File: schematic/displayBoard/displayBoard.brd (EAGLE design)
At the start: 65 x 65 mm, 30 parts, among them IC1 4028D, T1 MMBTA42, T10 MMBTA42, T2 MMBTA42, T3 MMBTA42, T4 MMBTA42, T5 MMBTA42, T6 MMBTA42, T7 MMBTA42, T8 MMBTA42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

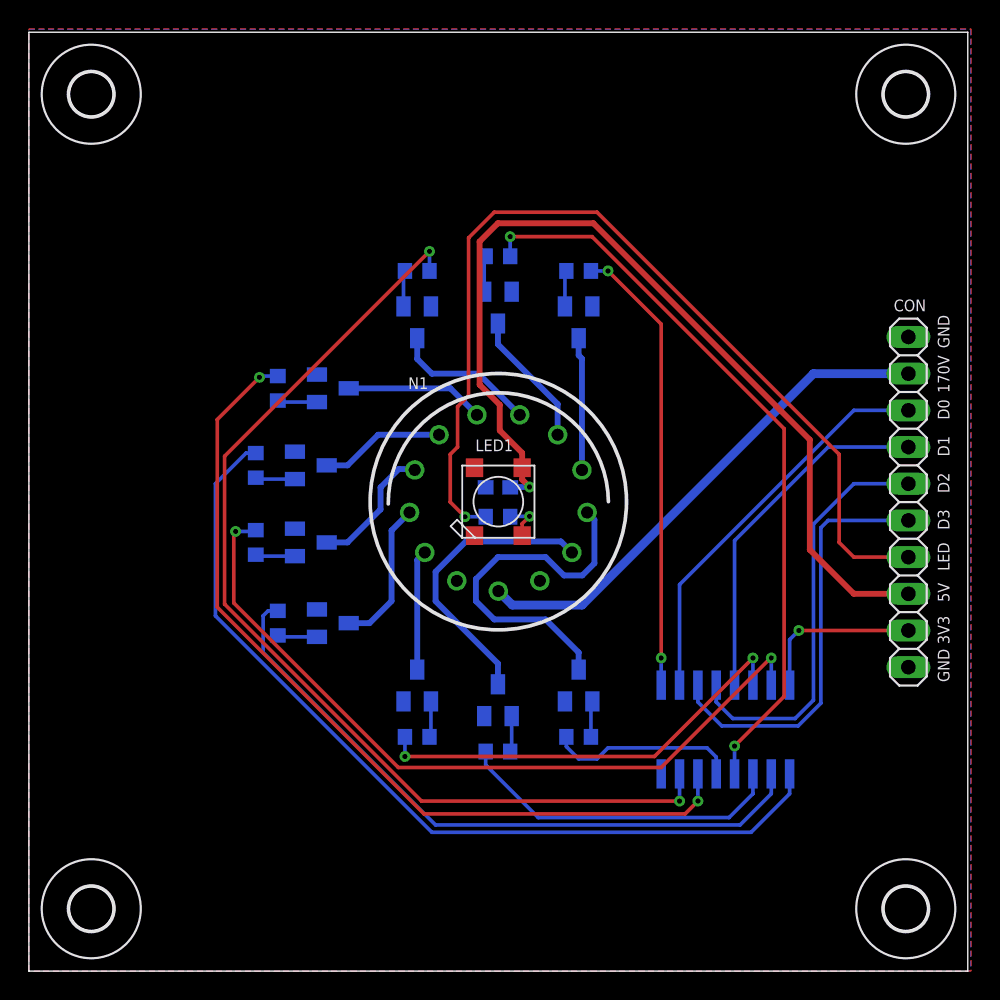
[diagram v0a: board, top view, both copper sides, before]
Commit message: Reduce the size of the controll board
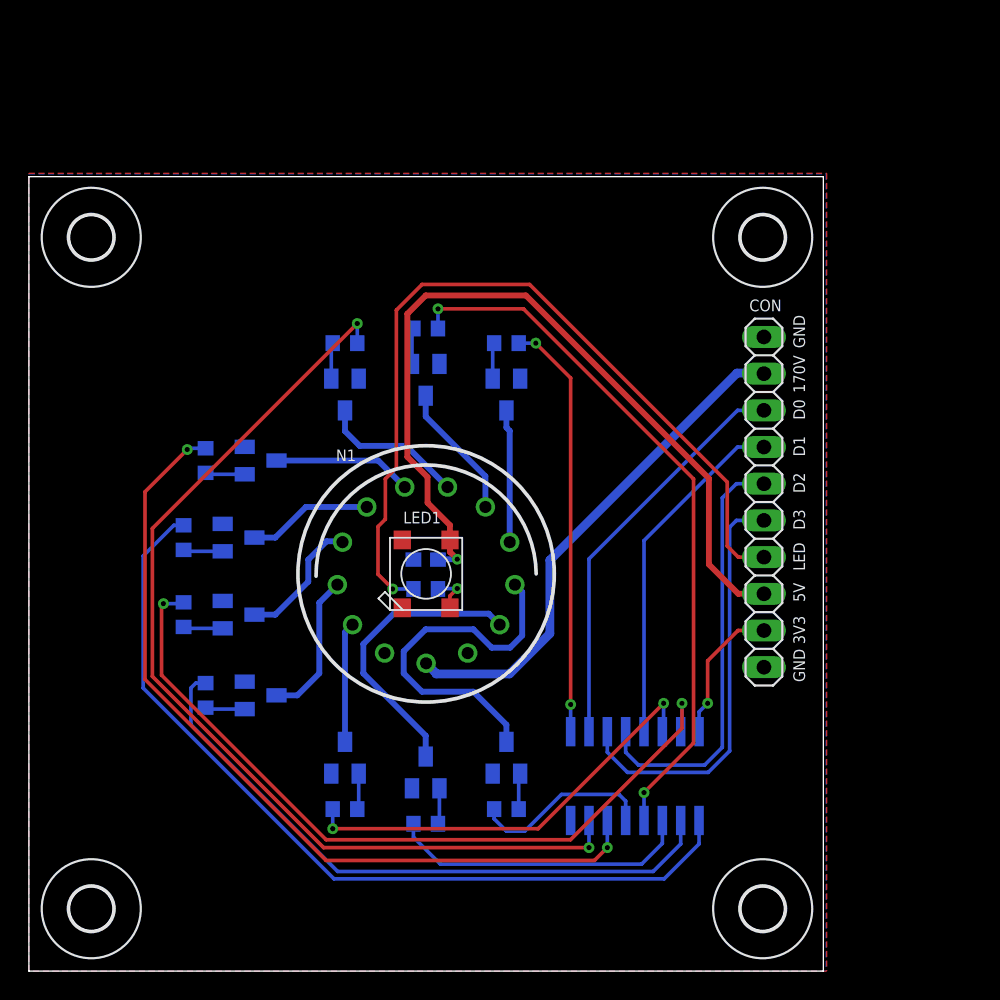
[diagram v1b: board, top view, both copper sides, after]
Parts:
- moved H1 14.0 mm to (50.8, 50.8)
- moved CON 10.0 mm to (50.9, 32.5)
- moved H2 9.91 mm to (4.32, 50.8)
- moved H4 9.91 mm to (50.8, 4.32)
- moved R10 7.07 mm to (33.1, 11.2)
- moved R2 7.07 mm to (21.9, 11.2)
- moved C1 7.07 mm to (27.5, 28.5)
- moved LED1 7.07 mm to (27.5, 27.5)
- moved N1 7.07 mm to (27.5, 27.5)
- moved R1 7.07 mm to (27.5, 10.2)
- moved R11 7.07 mm to (27.5, 26.5)
- moved R3 7.07 mm to (12.2, 19.1)
- moved R4 7.07 mm to (10.7, 24.7)
- moved R5 7.07 mm to (10.7, 30.0)
- moved R6 7.07 mm to (12.2, 35.3)
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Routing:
- net LED: track 66.3 -> 58.3 mm
- net +5V: track 65.1 -> 57.0 mm
- net DIG8: track 31.4 -> 29.1 mm
- net DIG7: track 51.1 -> 49.0 mm
- net DIG6: track 70.7 -> 68.7 mm
- net DIG5: track 59.9 -> 57.9 mm
- net DIG0: track 23.0 -> 21.1 mm
- net DIG4: track 61.3 -> 59.4 mm
- net DIG2: track 46.1 -> 44.2 mm
- net +3V3: track 11.6 -> 9.92 mm
- net D2: track 28.8 -> 29.5 mm
- net DIG3: track 53.4 -> 54.1 mm
- net D0: track 27.8 -> 28.3 mm
- net D1: track 24.7 -> 24.2 mm
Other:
- board size 65 x 65 mm -> 55 x 55 mm
